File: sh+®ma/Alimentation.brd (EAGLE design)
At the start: 171.4 x 101.3 mm, 17 parts, among them X1 87758-4016

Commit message: Carte mère (résolution problème transfo)
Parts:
- removed H1, H2: MOUNT-PAD-SQUARE3.0, holes:3,0-PAD-SQUARE
- removed TR1: (no value), trafo:EI54-1B
- added PAD1, PAD10, PAD2, PAD7, PAD8, PAD9: (no value), wirepad:2,54/1,1
- added SV1: (no value), con-lstb:MA20-2
- added X3, X4, X5, X6, X7, X8: (no value), con-molex:KK-156-4
- C2, C4: device rcl:C050-075X075 -> capacitor-wima:C22.5B6
- X1: value 87758-4016 -> TSW-101-02-S-Q; device con-molex:87758-4016 -> con-samtec:TSW-101-02-S-Q
- moved X1 154.3 mm to (5.00, 37.5)
- moved D1 67.3 mm to (123.2, 80.0), turned to 0 degrees
- moved R1 23.7 mm to (141.0, 45.7)
- moved C4 11.4 mm to (154.9, 22.9), turned to 90 degrees
- moved LM338K 10.2 mm to (123.2, 57.1)
- moved R2 9.67 mm to (143.5, 22.9), turned to 90 degrees
- moved C2 9.25 mm to (114.3, 27.9)
- moved D2 4.58 mm to (146.1, 44.5), turned to 90 degrees
- moved PAD6 1.37 mm to (70.0, 30.0)
- moved PAD5 1.33 mm to (70.0, 35.0)
- moved PAD4 1.29 mm to (70.0, 40.0)
- moved PAD3 1.25 mm to (70.0, 45.0)
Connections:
- removed net N$8 (its old number): C4.2, D1.A, D2.C, LM338K.3, R1.2, X1.2
- new net N$10: C4.2, D1.A, D2.C, LM338K.3, R1.2, SV1.39, X3.1, X4.1, X5.1, X6.1, X7.1, X8.1
- new net N$7: SV1.38, X3.3, X4.3, X5.3, X6.3, X7.3, X8.3
- new net N$9: SV1.40, X3.2, X4.2, X5.2, X6.2, X7.2, X8.2
- net N$1: now also PAD9.1, X1.2; no longer PAD4.1, TR1.13
- net N$2: now also PAD10.1, X1.1; no longer PAD5.1, TR1.9
- net N$3: now also SV1.35, X3.4, X4.4, X5.4, X6.4, X7.4, X8.4; no longer X1.6
- net N$5: now also PAD2.1, PAD4.1, PAD8.1; no longer H1.B3,0, TR1.1
- net N$6: now also PAD1.1, PAD5.1, PAD7.1; no longer H2.B3,0, TR1.7
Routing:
- net N$10: track 0.00 -> 356.2 mm, vias 0 -> 1
- net N$9: track 0.00 -> 291.9 mm, vias 0 -> 7
- net N$7: track 0.00 -> 261.0 mm, vias 0 -> 6
- net N$3: track 94.6 -> 350.4 mm
- net N$6: track 17.0 -> 75.2 mm
- net N$8: track 32.1 -> 77.6 mm
- net N$4: track 87.2 -> 118.0 mm
- net N$5: track 17.0 -> 40.6 mm
- net N$8 (its old number): track 20.6 -> 0.00 mm
- net N$1: track 26.7 -> 20.2 mm
- net N$2: track 25.5 -> 20.2 mm
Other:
- board size 171.4 x 101.3 mm -> 176.5 x 114 mm
- board text added: "GPIO"
- board text added: "Transformer"

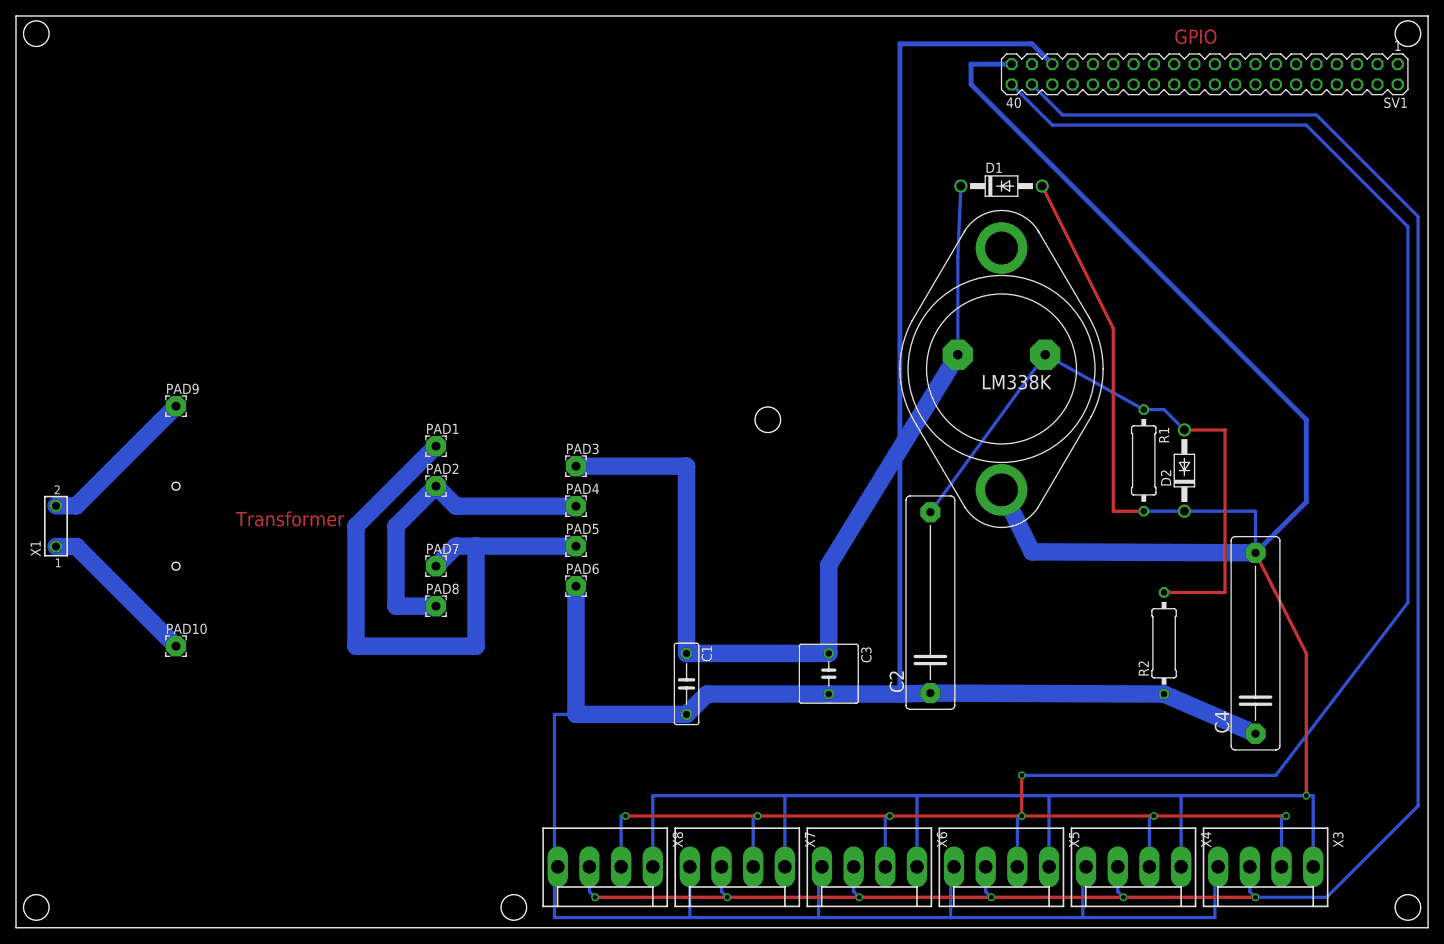
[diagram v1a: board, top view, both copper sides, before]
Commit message: Plan du soutien de l'écran + carte mère + écran
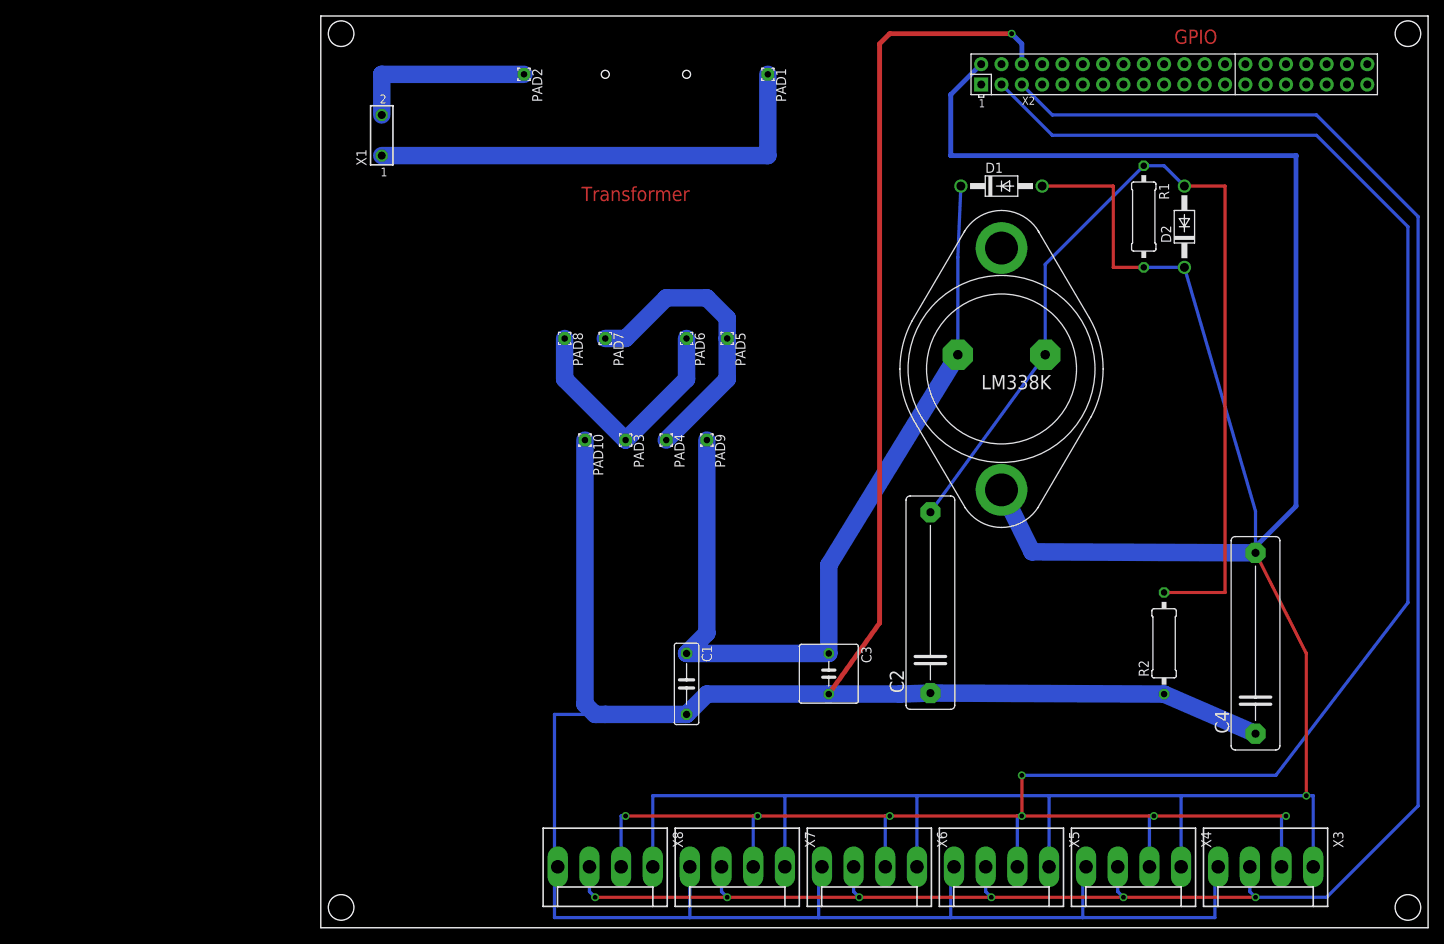
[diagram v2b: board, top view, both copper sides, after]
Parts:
- removed SV1: (no value), con-lstb:MA20-2
- added X2: RASPI_GPIO_B+#_PIN, raspberrypi_Bastelstube_v13:RASPI_GPIO_B+_PIN
- PAD1, PAD10, PAD2, PAD3, PAD4, PAD5, PAD6, PAD7, PAD8, PAD9: device wirepad:2,54/1,1 -> wirepad:1,6/0,8
- moved PAD9 66.5 mm to (86.4, 48.3), turned to 270 degrees
- moved X1 63.6 mm to (45.7, 86.4)
- moved PAD1 62.3 mm to (94.0, 94.0), turned to 270 degrees
- moved PAD10 57.2 mm to (71.1, 48.3), turned to 270 degrees
- moved PAD2 52.6 mm to (63.5, 94.0), turned to 270 degrees
- moved PAD8 37.1 mm to (68.6, 61.0), turned to 270 degrees
- moved PAD7 35.5 mm to (73.7, 61.0), turned to 270 degrees
- moved PAD6 33.9 mm to (83.8, 61.0), turned to 270 degrees
- moved PAD5 32.1 mm to (88.9, 61.0), turned to 270 degrees
- moved D2 30.5 mm to (146.1, 74.9)
- moved R1 30.5 mm to (141.0, 76.2)
- moved PAD4 14.0 mm to (81.3, 48.3), turned to 270 degrees
- moved PAD3 7.00 mm to (76.2, 48.3), turned to 270 degrees
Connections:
- new net 3V3A: X2.1
- new net 3V3B: X2.17
- new net 5V0B: X2.4
- new net GND_B: X2.9
- new net GND_C: X2.14
- new net GND_D: X2.20
- new net GND_E: X2.25
- new net GND_F: X2.30
- new net GND_G: X2.34
- new net GND_H: X2.39
- net N$1: now also PAD1.1, X1.1; no longer PAD9.1, X1.2
- net N$10: now also X2.2; no longer SV1.39
- net N$2: now also PAD2.1, X1.2; no longer PAD10.1, X1.1
- net N$3: now also PAD10.1, X2.6; no longer PAD6.1, SV1.35
- net N$4: now also PAD9.1; no longer PAD3.1
- net N$5: now also PAD3.1, PAD6.1; no longer PAD2.1, PAD4.1
- net N$6: now also PAD4.1; no longer PAD1.1
- net N$7: now also X2.5; no longer SV1.38
- net N$9: now also X2.3; no longer SV1.40
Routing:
- net N$8: track 77.6 -> 122.7 mm
- net N$6: track 75.2 -> 36.8 mm
- net N$1: track 20.2 -> 58.4 mm
- net N$3: track 350.4 -> 372.6 mm, vias 0 -> 1
- net N$10: track 356.2 -> 377.2 mm
- net N$4: track 118.0 -> 108.5 mm
- net N$5: track 40.6 -> 31.7 mm
- net N$2: track 20.2 -> 22.9 mm
- net N$9: track 291.9 -> 293.2 mm
- net N$7: track 261.0 -> 262.3 mm
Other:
- board size 176.5 x 114 mm -> 138.4 x 114 mm

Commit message: typon + plaque fond
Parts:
- removed X4, X6, X7, X8: (no value), con-molex:KK-156-4
- added R3, R4: 220, rcl:0309/12
- added SV1: (no value), con-lsta:FE08
- added X10, X11, X12, X13, X14, X9: MKS1854-6-0-404, con-stocko:MKS1854-6-0-404
- PAD1, PAD10, PAD2, PAD3, PAD4, PAD5, PAD6, PAD7, PAD8, PAD9: value (none) -> WIREPAD3,17/1,3; device wirepad:1,6/0,8 -> wirepad:3,17/1,3
- R2: value 660 -> 220
- X3: value (none) -> MKS1854-6-0-404; device con-molex:KK-156-4 -> con-stocko:MKS1854-6-0-404
- X5: value (none) -> MKS1852-6-0-202; device con-molex:KK-156-4 -> con-stocko:MKS1852-6-0-202
- moved X3 85.1 mm to (71.1, -2.54), turned to 90 degrees
- moved X5 80.8 mm to (53.3, 35.6)
- moved D2 5.08 mm to (146.1, 69.8), turned to 270 degrees
- moved R1 5.08 mm to (141.0, 71.1), turned to 90 degrees
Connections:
- new net N$11: R3.2, R4.1
- new net N$12: SV1.5, X10.2, X11.2, X12.2, X13.2, X14.2, X2.5, X3.2, X9.2
- net N$10: now also SV1.1, X10.4, X11.4, X12.4, X13.4, X14.4, X3.4, X5.2, X9.4; no longer X3.1, X4.1, X5.1, X6.1, X7.1, X8.1
- net N$3: now also SV1.2, X10.1, X11.1, X12.1, X13.1, X14.1, X3.1, X5.1, X9.1; no longer X3.4, X4.4, X5.4, X6.4, X7.4, X8.4
- net N$7: now also SV1.6, X10.3, X11.3, X12.3, X13.3, X14.3, X2.3, X9.3; no longer X2.5, X4.3, X5.3, X6.3, X7.3, X8.3
- net N$8: now also R4.2; no longer R2.2
- net N$9: now also R2.2, R3.1; no longer X2.3, X3.2, X4.2, X5.2, X6.2, X7.2, X8.2
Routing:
- net N$9: track 293.2 -> 6.35 mm, vias 7 -> 0
- net N$12: track 0.00 -> 260.9 mm
- net N$3: track 372.6 -> 446.0 mm, vias 1 -> 0
- net N$8: track 122.7 -> 66.6 mm
- net N$10: track 377.2 -> 426.5 mm
- net N$11: track 0.00 -> 16.3 mm
- net N$7: track 262.3 -> 257.3 mm, vias 6 -> 0
- net N$4: track 108.5 -> 110.8 mm
